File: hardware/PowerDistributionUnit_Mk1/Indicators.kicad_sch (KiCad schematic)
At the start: 60 parts, among them J13 Logic Analyzer, SW1 JS202011SCQN, U27 74LVC594APW,118, U28 74LVC594APW,118, U29 74AUP1G04GW-Q100H, U30 NL27WZ17DFT2G-Q

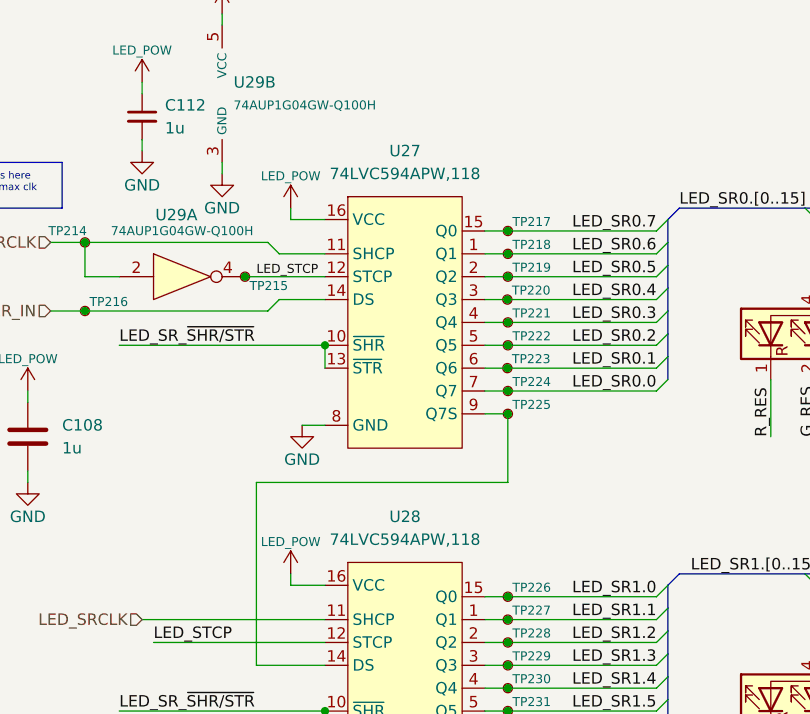
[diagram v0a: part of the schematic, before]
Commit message: correct SR part number to SOIC package
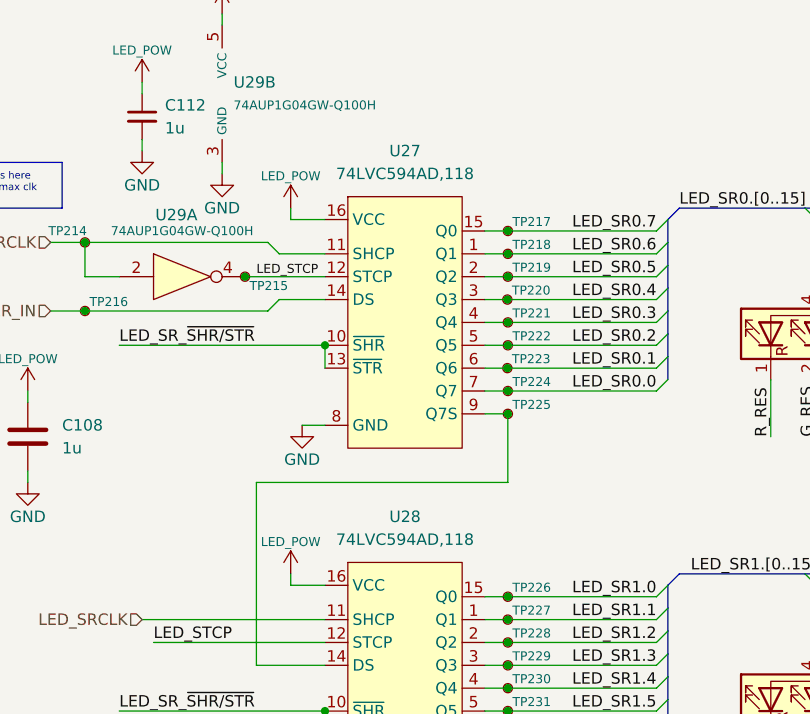
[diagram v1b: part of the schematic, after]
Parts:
- U27, U28: value 74LVC594APW,118 -> 74LVC594AD,118; symbol PowerDistributionUnitLib:74LVC594APW,118 -> PowerDistributionUnitLib:74LVC594AD,118; Digikey P/N 1727-6687-1-ND -> 1727-74LVC594AD,118CT-ND; LCSC P/N C548830 -> C548827; Mouser P/N 771-LVC594APW118 -> 771-LVC594AD118; P/N 74LVC594APW,118 -> 74LVC594AD,118
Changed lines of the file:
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@@
 	)
 	(symbol
-		(lib_id "PowerDistributionUnitLib:74LVC594APW,118")
+		(lib_id "PowerDistributionUnitLib:74LVC594AD,118")
 		(at 78.74 101.6 0)
 		(unit 1)
@@
 			)
 		)
-		(property "Value" "74LVC594APW,118"
+		(property "Value" "74LVC594AD,118"
 			(at 78.74 85.09 0)
 			(effects
@@
 			)
 		)
-		(property "P/N" "74LVC594APW,118"
+		(property "P/N" "74LVC594AD,118"
 			(at 78.74 101.6 0)
 			(effects
@@
 			)
 		)
-		(property "Mouser P/N" "771-LVC594APW118"
+		(property "Mouser P/N" "771-LVC594AD118"
 			(at 78.74 101.6 0)
 			(effects
@@
 			)
 		)
-		(property "Digikey P/N" "1727-6687-1-ND"
+		(property "Digikey P/N" "1727-74LVC594AD,118CT-ND"
 			(at 78.74 101.6 0)
 			(effects
@@
 			)
 		)
-		(property "LCSC P/N" "C548830"
+		(property "LCSC P/N" "C548827"
 			(at 78.74 101.6 0)
 			(effects
@@
 	)
 	(symbol
-		(lib_id "PowerDistributionUnitLib:74LVC594APW,118")
+		(lib_id "PowerDistributionUnitLib:74LVC594AD,118")
 		(at 78.74 142.24 0)
 		(unit 1)
@@
 			)
 		)
-		(property "Value" "74LVC594APW,118"
+		(property "Value" "74LVC594AD,118"
 			(at 78.74 125.73 0)
 			(effects
@@
 			)
 		)
-		(property "P/N" "74LVC594APW,118"
+		(property "P/N" "74LVC594AD,118"
 			(at 78.74 142.24 0)
 			(effects
@@
 			)
 		)
-		(property "Mouser P/N" "771-LVC594APW118"
+		(property "Mouser P/N" "771-LVC594AD118"
 			(at 78.74 142.24 0)
 			(effects
@@
 			)
 		)
-		(property "Digikey P/N" "1727-6687-1-ND"
+		(property "Digikey P/N" "1727-74LVC594AD,118CT-ND"
 			(at 78.74 142.24 0)
 			(effects
@@
 			)
 		)
-		(property "LCSC P/N" "C548830"
+		(property "LCSC P/N" "C548827"
 			(at 78.74 142.24 0)
 			(effects
